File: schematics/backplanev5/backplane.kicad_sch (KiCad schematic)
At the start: 0 parts

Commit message: Update
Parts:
- added J1, J10, J2, J3, J4, J5, J6, J7, J8, J9: ~, ConnPdSilva:conn_euro96, symbol ConnPdSilva:ConnEuro96
- added J11, J12, J13, J14: Conn_01x02, Connector_PinHeader_2.54mm:PinHeader_2x01_P2.54mm_Vertical, symbol Connector_Generic:Conn_01x02
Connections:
- new net +12V: J1.92, J10.92, J13.1 (Pin_1), J2.92, J3.92, J4.92, J5.92, J6.92, J7.92, J8.92, J9.92
- new net +5V: J1.1, J1.33, J1.65, J10.1, J10.33, J10.65, J11.1 (Pin_1), J14.1 (Pin_1), J2.1, J2.33, J2.65, J3.1, J3.33, J3.65, J4.1, J4.33, J4.65, J5.1, J5.33, J5.65, J6.1, J6.33, J6.65, J7.1, J7.33, J7.65, J8.1, J8.33, J8.65, J9.1, J9.33, J9.65
- new net -5V: J1.94, J10.94, J12.1 (Pin_1), J2.94, J3.94, J4.94, J5.94, J6.94, J7.94, J8.94, J9.94
- new net A0: J1.18, J10.18, J2.18, J3.18, J4.18, J5.18, J6.18, J7.18, J8.18, J9.18
- new net A1: J1.19, J10.19, J2.19, J3.19, J4.19, J5.19, J6.19, J7.19, J8.19, J9.19
- new net A10: J1.28, J10.28, J2.28, J3.28, J4.28, J5.28, J6.28, J7.28, J8.28, J9.28
- new net A11: J1.29, J10.29, J2.29, J3.29, J4.29, J5.29, J6.29, J7.29, J8.29, J9.29
- new net A12: J1.30, J10.30, J2.30, J3.30, J4.30, J5.30, J6.30, J7.30, J8.30, J9.30
- new net A13: J1.31, J10.31, J2.31, J3.31, J4.31, J5.31, J6.31, J7.31, J8.31, J9.31
- new net A14: J1.63, J10.63, J2.63, J3.63, J4.63, J5.63, J6.63, J7.63, J8.63, J9.63
- new net A15: J1.62, J10.62, J2.62, J3.62, J4.62, J5.62, J6.62, J7.62, J8.62, J9.62
- new net A16: J1.61, J10.61, J2.61, J3.61, J4.61, J5.61, J6.61, J7.61, J8.61, J9.61
- new net A17: J1.60, J10.60, J2.60, J3.60, J4.60, J5.60, J6.60, J7.60, J8.60, J9.60
- new net A18: J1.59, J10.59, J2.59, J3.59, J4.59, J5.59, J6.59, J7.59, J8.59, J9.59
- new net A19: J1.58, J10.58, J2.58, J3.58, J4.58, J5.58, J6.58, J7.58, J8.58, J9.58
- new net A2: J1.20, J10.20, J2.20, J3.20, J4.20, J5.20, J6.20, J7.20, J8.20, J9.20
- new net A20: J1.57, J10.57, J2.57, J3.57, J4.57, J5.57, J6.57, J7.57, J8.57, J9.57
- new net A21: J1.56, J10.56, J2.56, J3.56, J4.56, J5.56, J6.56, J7.56, J8.56, J9.56
- new net A22: J1.55, J10.55, J2.55, J3.55, J4.55, J5.55, J6.55, J7.55, J8.55, J9.55
- new net A3: J1.21, J10.21, J2.21, J3.21, J4.21, J5.21, J6.21, J7.21, J8.21, J9.21
- new net A4: J1.22, J10.22, J2.22, J3.22, J4.22, J5.22, J6.22, J7.22, J8.22, J9.22
- new net A5: J1.23, J10.23, J2.23, J3.23, J4.23, J5.23, J6.23, J7.23, J8.23, J9.23
- new net A6: J1.24, J10.24, J2.24, J3.24, J4.24, J5.24, J6.24, J7.24, J8.24, J9.24
- new net A7: J1.25, J10.25, J2.25, J3.25, J4.25, J5.25, J6.25, J7.25, J8.25, J9.25
- new net A8: J1.26, J10.26, J2.26, J3.26, J4.26, J5.26, J6.26, J7.26, J8.26, J9.26
- new net A9: J1.27, J10.27, J2.27, J3.27, J4.27, J5.27, J6.27, J7.27, J8.27, J9.27
- new net ALE: J1.73, J10.73, J2.73, J3.73, J4.73, J5.73, J6.73, J7.73, J8.73, J9.73
- new net CRUCLK: J1.35, J10.35, J2.35, J3.35, J4.35, J5.35, J6.35, J7.35, J8.35, J9.35
- new net CRUIN: J1.36, J10.36, J2.36, J3.36, J4.36, J5.36, J6.36, J7.36, J8.36, J9.36
- new net CRUOUT: J1.37, J10.37, J2.37, J3.37, J4.37, J5.37, J6.37, J7.37, J8.37, J9.37
- new net D0: J1.2, J10.2, J2.2, J3.2, J4.2, J5.2, J6.2, J7.2, J8.2, J9.2
- new net D1: J1.3, J10.3, J2.3, J3.3, J4.3, J5.3, J6.3, J7.3, J8.3, J9.3
- new net D10: J1.12, J10.12, J2.12, J3.12, J4.12, J5.12, J6.12, J7.12, J8.12, J9.12
- new net D11: J1.13, J10.13, J2.13, J3.13, J4.13, J5.13, J6.13, J7.13, J8.13, J9.13
- new net D12: J1.14, J10.14, J2.14, J3.14, J4.14, J5.14, J6.14, J7.14, J8.14, J9.14
- new net D13: J1.15, J10.15, J2.15, J3.15, J4.15, J5.15, J6.15, J7.15, J8.15, J9.15
- new net D14: J1.16, J10.16, J2.16, J3.16, J4.16, J5.16, J6.16, J7.16, J8.16, J9.16
- new net D15: J1.17, J10.17, J2.17, J3.17, J4.17, J5.17, J6.17, J7.17, J8.17, J9.17
- new net D2: J1.4, J10.4, J2.4, J3.4, J4.4, J5.4, J6.4, J7.4, J8.4, J9.4
- new net D3: J1.5, J10.5, J2.5, J3.5, J4.5, J5.5, J6.5, J7.5, J8.5, J9.5
- new net D4: J1.6, J10.6, J2.6, J3.6, J4.6, J5.6, J6.6, J7.6, J8.6, J9.6
- new net D5: J1.7, J10.7, J2.7, J3.7, J4.7, J5.7, J6.7, J7.7, J8.7, J9.7
- new net D6: J1.8, J10.8, J2.8, J3.8, J4.8, J5.8, J6.8, J7.8, J8.8, J9.8
- new net D7: J1.9, J10.9, J2.9, J3.9, J4.9, J5.9, J6.9, J7.9, J8.9, J9.9
- new net D8: J1.10, J10.10, J2.10, J3.10, J4.10, J5.10, J6.10, J7.10, J8.10, J9.10
- new net D9: J1.11, J10.11, J2.11, J3.11, J4.11, J5.11, J6.11, J7.11, J8.11, J9.11
- new net DBIN: J1.38, J10.38, J2.38, J3.38, J4.38, J5.38, J6.38, J7.38, J8.38, J9.38
- new net DT/R: J1.75, J10.75, J2.75, J3.75, J4.75, J5.75, J6.75, J7.75, J8.75, J9.75
- new net E: J1.34, J10.34, J2.34, J3.34, J4.34, J5.34, J6.34, J7.34, J8.34, J9.34
- new net GND: J1.32, J1.64, J1.93, J1.95, J1.96, J10.32, J10.64, J10.93, J10.95, J10.96, J11.2 (Pin_2), J12.2 (Pin_2), J13.2 (Pin_2), J14.2 (Pin_2), J2.32, J2.64, J2.93, J2.95, J2.96, J3.32, J3.64, J3.93, J3.95, J3.96, J4.32, J4.64, J4.93, J4.95, J4.96, J5.32, J5.64, J5.93, J5.95, J5.96, J6.32, J6.64, J6.93, J6.95, J6.96, J7.32, J7.64, J7.93, J7.95, J7.96, J8.32, J8.64, J8.93, J8.95, J8.96, J9.32, J9.64, J9.93, J9.95, J9.96
- new net HLDA: J1.52, J10.52, J2.52, J3.52, J4.52, J5.52, J6.52, J7.52, J8.52, J9.52
- new net IAQ: J1.39, J10.39, J2.39, J3.39, J4.39, J5.39, J6.39, J7.39, J8.39, J9.39
- new net IC3: J1.47, J10.47, J2.47, J3.47, J4.47, J5.47, J6.47, J7.47, J8.47, J9.47
- new net IPL0: J1.50, J10.50, J2.50, J3.50, J4.50, J5.50, J6.50, J7.50, J8.50, J9.50
- new net IPL1: J1.49, J10.49, J2.49, J3.49, J4.49, J5.49, J6.49, J7.49, J8.49, J9.49
- new net IPL2: J1.48, J10.48, J2.48, J3.48, J4.48, J5.48, J6.48, J7.48, J8.48, J9.48
- new net M/IO: J1.76, J10.76, J2.76, J3.76, J4.76, J5.76, J6.76, J7.76, J8.76, J9.76
- new net NMI: J1.41, J10.41, J2.41, J3.41, J4.41, J5.41, J6.41, J7.41, J8.41, J9.41
- new net RDY: J1.44, J10.44, J2.44, J3.44, J4.44, J5.44, J6.44, J7.44, J8.44, J9.44
- new net Res1: J1.81, J10.81, J2.81, J3.81, J4.81, J5.81, J6.81, J7.81, J8.81, J9.81
- new net Res10: J1.90, J10.90, J2.90, J3.90, J4.90, J5.90, J6.90, J7.90, J8.90, J9.90
- new net Res11: J1.91, J10.91, J2.91, J3.91, J4.91, J5.91, J6.91, J7.91, J8.91, J9.91
- new net Res12: J1.54, J10.54, J2.54, J3.54, J4.54, J5.54, J6.54, J7.54, J8.54, J9.54
- new net Res2: J1.82, J10.82, J2.82, J3.82, J4.82, J5.82, J6.82, J7.82, J8.82, J9.82
- new net Res3: J1.83, J10.83, J2.83, J3.83, J4.83, J5.83, J6.83, J7.83, J8.83, J9.83
- new net Res4: J1.84, J10.84, J2.84, J3.84, J4.84, J5.84, J6.84, J7.84, J8.84, J9.84
- new net Res5: J1.85, J10.85, J2.85, J3.85, J4.85, J5.85, J6.85, J7.85, J8.85, J9.85
- new net Res6: J1.86, J10.86, J2.86, J3.86, J4.86, J5.86, J6.86, J7.86, J8.86, J9.86
- new net Res7: J1.87, J10.87, J2.87, J3.87, J4.87, J5.87, J6.87, J7.87, J8.87, J9.87
- new net Res8: J1.88, J10.88, J2.88, J3.88, J4.88, J5.88, J6.88, J7.88, J8.88, J9.88
- new net Res9: J1.89, J10.89, J2.89, J3.89, J4.89, J5.89, J6.89, J7.89, J8.89, J9.89
- new net /AS: J1.43, J10.43, J2.43, J3.43, J4.43, J5.43, J6.43, J7.43, J8.43, J9.43
- new net /BERR: J1.68, J10.68, J2.68, J3.68, J4.68, J5.68, J6.68, J7.68, J8.68, J9.68
- new net /BGACK: J1.69, J10.69, J2.69, J3.69, J4.69, J5.69, J6.69, J7.69, J8.69, J9.69
- new net /DEN: J1.74, J10.74, J2.74, J3.74, J4.74, J5.74, J6.74, J7.74, J8.74, J9.74
- new net /HALT: J1.53, J10.53, J2.53, J3.53, J4.53, J5.53, J6.53, J7.53, J8.53, J9.53
- new net /HOLD: J1.42, J10.42, J2.42, J3.42, J4.42, J5.42, J6.42, J7.42, J8.42, J9.42
- new net /INTA: J1.72, J10.72, J2.72, J3.72, J4.72, J5.72, J6.72, J7.72, J8.72, J9.72
- new net /INTR: J1.40, J10.40, J2.40, J3.40, J4.40, J5.40, J6.40, J7.40, J8.40, J9.40
- new net /LDS: J1.70, J10.70, J2.70, J3.70, J4.70, J5.70, J6.70, J7.70, J8.70, J9.70
- new net /M1: J1.79, J10.79, J2.79, J3.79, J4.79, J5.79, J6.79, J7.79, J8.79, J9.79
- new net /RD: J1.45, J10.45, J2.45, J3.45, J4.45, J5.45, J6.45, J7.45, J8.45, J9.45
- new net /RFSH: J1.80, J10.80, J2.80, J3.80, J4.80, J5.80, J6.80, J7.80, J8.80, J9.80
- new net /RST: J1.51, J10.51, J2.51, J3.51, J4.51, J5.51, J6.51, J7.51, J8.51, J9.51
- new net /SSO: J1.77, J10.77, J2.77, J3.77, J4.77, J5.77, J6.77, J7.77, J8.77, J9.77
- new net /UDS: J1.71, J10.71, J2.71, J3.71, J4.71, J5.71, J6.71, J7.71, J8.71, J9.71
- new net /VMA: J1.66, J10.66, J2.66, J3.66, J4.66, J5.66, J6.66, J7.66, J8.66, J9.66
- new net /VPA: J1.67, J10.67, J2.67, J3.67, J4.67, J5.67, J6.67, J7.67, J8.67, J9.67
- new net /WAIT: J1.78, J10.78, J2.78, J3.78, J4.78, J5.78, J6.78, J7.78, J8.78, J9.78
- new net /WE: J1.46, J10.46, J2.46, J3.46, J4.46, J5.46, J6.46, J7.46, J8.46, J9.46

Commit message: Update V1 fabrication 04-12-2025 JLCPCB
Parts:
- added H1, H2, H3, H4, H5, H6: MountingHole, MountingHole:MountingHole_3.2mm_M3, symbol Mechanical:MountingHole

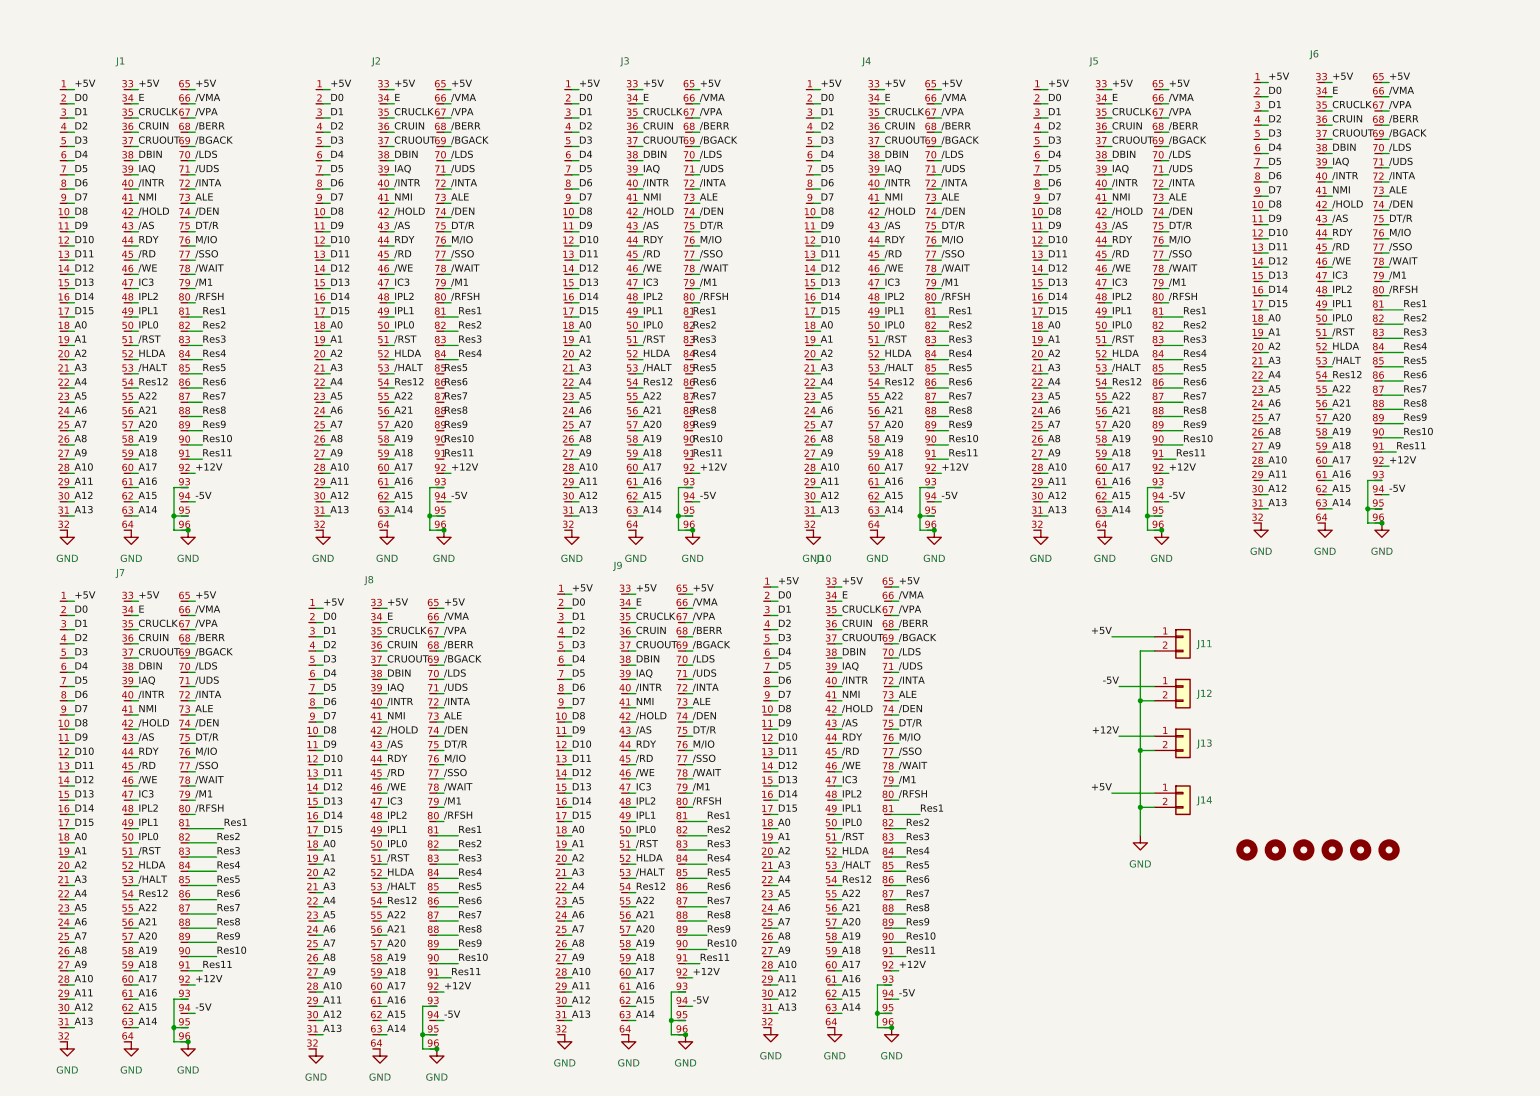
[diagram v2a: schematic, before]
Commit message: Terminada as mudancas falta agora fazer oDRC
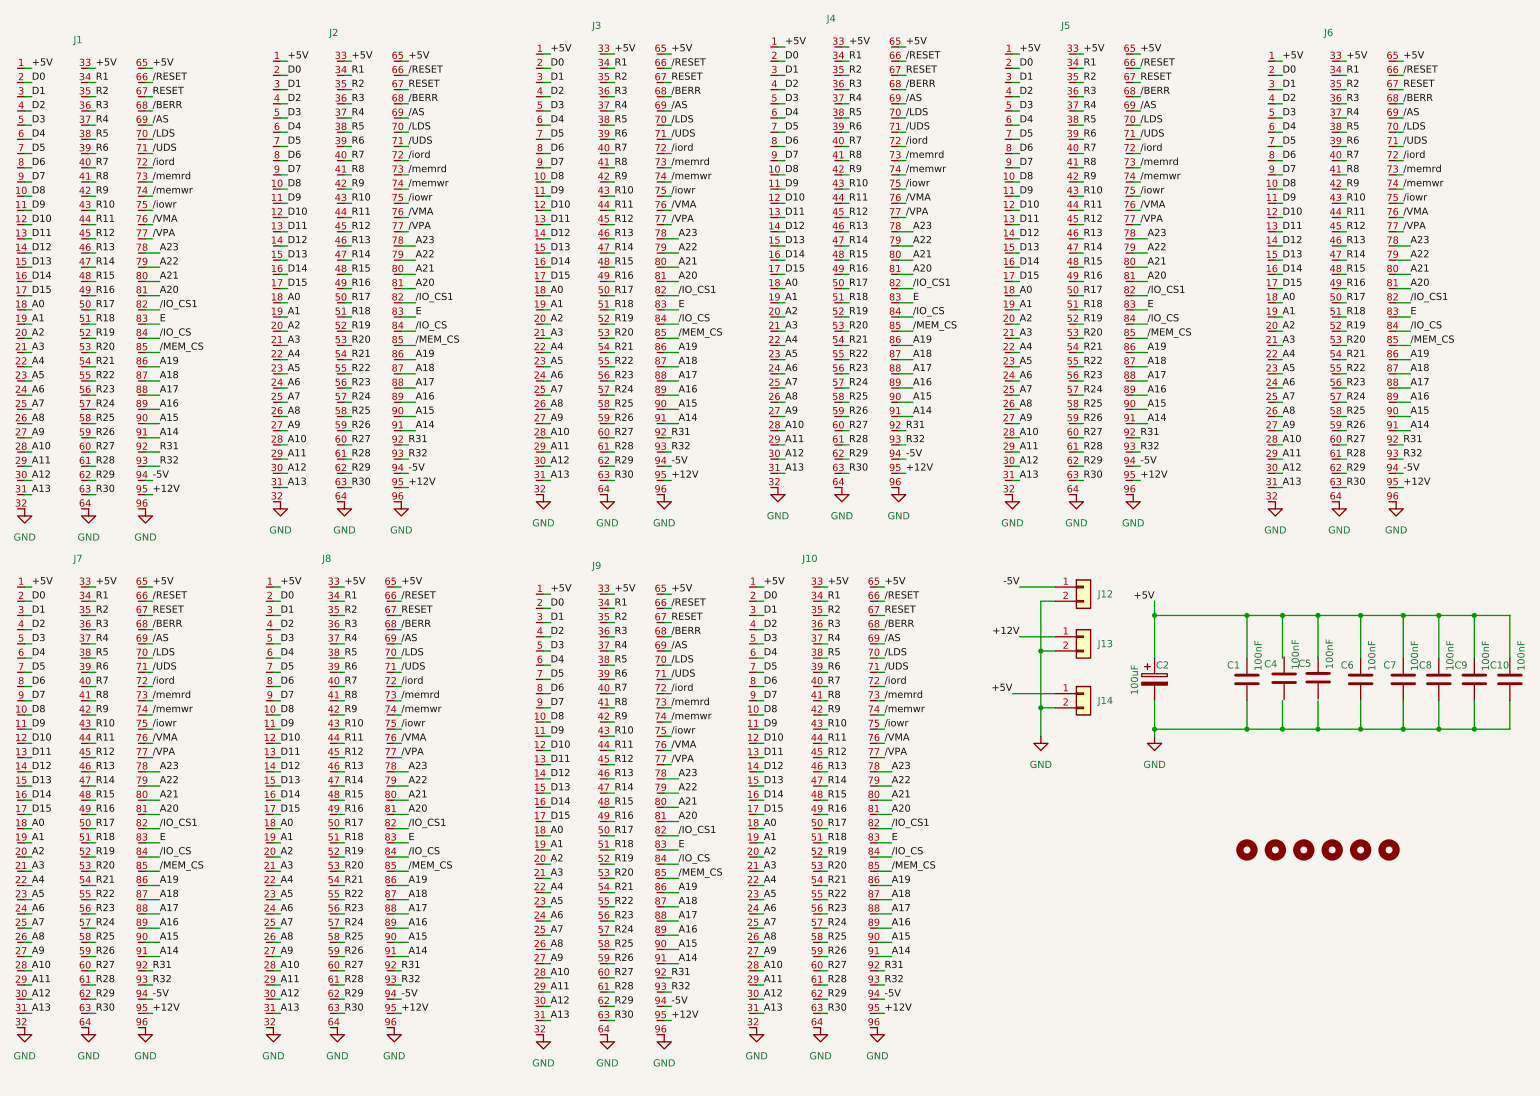
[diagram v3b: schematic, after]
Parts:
- removed J11: Conn_01x02, Connector_PinHeader_2.54mm:PinHeader_2x01_P2.54mm_Vertical, symbol Connector_Generic:Conn_01x02
- added C1, C10, C4, C5, C6, C7, C8, C9: 100nF, Capacitor_THT:C_Disc_D4.3mm_W1.9mm_P5.00mm, symbol Device:C
- added C2: 100uF, Capacitor_THT:CP_Radial_D8.0mm_P5.00mm, symbol Device:C_Polarized
- J12, J13, J14: footprint Connector_PinHeader_2.54mm:PinHeader_2x01_P2.54mm_Vertical -> TerminalBlock_Phoenix:TerminalBlock_Phoenix_MKDS-1,5-2-5.08_1x02_P5.08mm_Horizontal
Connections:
- net M/IO is gone; now on net /VMA: J1.76, J10.76, J2.76, J3.76, J4.76, J5.76, J6.76, J7.76, J8.76, J9.76
- net Res1 is gone; now on net A20: J1.81, J10.81, J2.81, J3.81, J4.81, J5.81, J6.81, J7.81, J8.81, J9.81
- net Res10 is gone; now on net A15: J1.90, J10.90, J2.90, J3.90, J4.90, J5.90, J6.90, J7.90, J8.90, J9.90
- net Res11 is gone; now on net A14: J1.91, J10.91, J2.91, J3.91, J4.91, J5.91, J6.91, J7.91, J8.91, J9.91
- net Res3 is gone; now on net E: J1.83, J10.83, J2.83, J3.83, J4.83, J5.83, J6.83, J7.83, J8.83, J9.83
- net Res6 is gone; now on net A19: J1.86, J10.86, J2.86, J3.86, J4.86, J5.86, J6.86, J7.86, J8.86, J9.86
- net Res7 is gone; now on net A18: J1.87, J10.87, J2.87, J3.87, J4.87, J5.87, J6.87, J7.87, J8.87, J9.87
- net Res8 is gone; now on net A17: J1.88, J10.88, J2.88, J3.88, J4.88, J5.88, J6.88, J7.88, J8.88, J9.88
- net Res9 is gone; now on net A16: J1.89, J10.89, J2.89, J3.89, J4.89, J5.89, J6.89, J7.89, J8.89, J9.89
- net /BGACK is gone; now on net /AS: J1.69, J10.69, J2.69, J3.69, J4.69, J5.69, J6.69, J7.69, J8.69, J9.69
- net /M1 is gone; now on net A22: J1.79, J10.79, J2.79, J3.79, J4.79, J5.79, J6.79, J7.79, J8.79, J9.79
- net /RFSH is gone; now on net A21: J1.80, J10.80, J2.80, J3.80, J4.80, J5.80, J6.80, J7.80, J8.80, J9.80
- net /SSO is gone; now on net /VPA: J1.77, J10.77, J2.77, J3.77, J4.77, J5.77, J6.77, J7.77, J8.77, J9.77
- net +12V: now also J1.95, J10.95, J2.95, J3.95, J4.95, J5.95, J6.95, J7.95, J8.95, J9.95; no longer J1.92, J10.92, J2.92, J3.92, J4.92, J5.92, J6.92, J7.92, J8.92, J9.92
- net +5V: now also C1.1, C10.1, C2.1, C6.1, C7.1, C8.1, C9.1
- net A14: no longer J1.63, J10.63, J2.63, J3.63, J4.63, J5.63, J6.63, J7.63, J8.63, J9.63
- net A15: no longer J1.62, J10.62, J2.62, J3.62, J4.62, J5.62, J6.62, J7.62, J8.62, J9.62
- net A16: no longer J1.61, J10.61, J2.61, J3.61, J4.61, J5.61, J6.61, J7.61, J8.61, J9.61
- net A17: no longer J1.60, J10.60, J2.60, J3.60, J4.60, J5.60, J6.60, J7.60, J8.60, J9.60
- net A18: no longer J1.59, J10.59, J2.59, J3.59, J4.59, J5.59, J6.59, J7.59, J8.59, J9.59
- net A19: no longer J1.58, J10.58, J2.58, J3.58, J4.58, J5.58, J6.58, J7.58, J8.58, J9.58
- net A20: no longer J1.57, J10.57, J2.57, J3.57, J4.57, J5.57, J6.57, J7.57, J8.57, J9.57
- net A21: no longer J1.56, J10.56, J2.56, J3.56, J4.56, J5.56, J6.56, J7.56, J8.56, J9.56
- net A22: no longer J1.55, J10.55, J2.55, J3.55, J4.55, J5.55, J6.55, J7.55, J8.55, J9.55
- net E: no longer J1.34, J10.34, J2.34, J3.34, J4.34, J5.34, J6.34, J7.34, J8.34, J9.34
- net GND: now also C1.2, C10.2, C2.2, C6.2, C7.2, C8.2, C9.2; no longer J1.93, J1.95, J10.93, J10.95, J2.93, J2.95, J3.93, J3.95, J4.93, J4.95, J5.93, J5.95, J6.93, J6.95, J7.93, J7.95, J8.93, J8.95, J9.93, J9.95
- net /AS: no longer J1.43, J10.43, J2.43, J3.43, J4.43, J5.43, J6.43, J7.43, J8.43, J9.43
- net /VMA: no longer J1.66, J10.66, J2.66, J3.66, J4.66, J5.66, J6.66, J7.66, J8.66, J9.66
- net /VPA: no longer J1.67, J10.67, J2.67, J3.67, J4.67, J5.67, J6.67, J7.67, J8.67, J9.67
- net ALE renamed /memrd
- net CRUCLK renamed R2
- net CRUIN renamed R3
- net CRUOUT renamed R4
- net DBIN renamed R5
- net DT/R renamed /iowr
- net HLDA renamed R19
- net IAQ renamed R6
- net IC3 renamed R14
- net IPL0 renamed R17
- net IPL1 renamed R16
- net IPL2 renamed R15
- net NMI renamed R8
- net RDY renamed R11
- net Res12 renamed R21
- net Res2 renamed /IO_CS1
- net Res4 renamed /IO_CS
- net Res5 renamed /MEM_CS
- net /DEN renamed /memwr
- net /HALT renamed R20
- net /HOLD renamed R9
- net /INTA renamed /iord
- net /INTR renamed R7
- net /RD renamed R12
- net /RST renamed R18
- net /WAIT renamed A23
- net /WE renamed R13
- new net R1: J1.34, J10.34, J2.34, J3.34, J4.34, J5.34, J6.34, J7.34, J8.34, J9.34
- new net R10: J1.43, J10.43, J2.43, J3.43, J4.43, J5.43, J6.43, J7.43, J8.43, J9.43
- new net R22: J1.55, J10.55, J2.55, J3.55, J4.55, J5.55, J6.55, J7.55, J8.55, J9.55
- new net R23: J1.56, J10.56, J2.56, J3.56, J4.56, J5.56, J6.56, J7.56, J8.56, J9.56
- new net R24: J1.57, J10.57, J2.57, J3.57, J4.57, J5.57, J6.57, J7.57, J8.57, J9.57
- new net R25: J1.58, J10.58, J2.58, J3.58, J4.58, J5.58, J6.58, J7.58, J8.58, J9.58
- new net R26: J1.59, J10.59, J2.59, J3.59, J4.59, J5.59, J6.59, J7.59, J8.59, J9.59
- new net R27: J1.60, J10.60, J2.60, J3.60, J4.60, J5.60, J6.60, J7.60, J8.60, J9.60
- new net R28: J1.61, J10.61, J2.61, J3.61, J4.61, J5.61, J6.61, J7.61, J8.61, J9.61
- new net R29: J1.62, J10.62, J2.62, J3.62, J4.62, J5.62, J6.62, J7.62, J8.62, J9.62
- new net R30: J1.63, J10.63, J2.63, J3.63, J4.63, J5.63, J6.63, J7.63, J8.63, J9.63
- new net R31: J1.92, J10.92, J2.92, J3.92, J4.92, J5.92, J6.92, J7.92, J8.92, J9.92
- new net R32: J1.93, J10.93, J2.93, J3.93, J4.93, J5.93, J6.93, J7.93, J8.93, J9.93
- new net RESET: J1.67, J10.67, J2.67, J3.67, J4.67, J5.67, J6.67, J7.67, J8.67, J9.67
- new net /RESET: J1.66, J10.66, J2.66, J3.66, J4.66, J5.66, J6.66, J7.66, J8.66, J9.66
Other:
- moved on the sheet: J1, J12, J13, J14

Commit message: Terminado o DRC
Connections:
- net +5V: now also C4.1, C5.1
- net GND: now also C4.2, C5.2
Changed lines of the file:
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@@
 	(symbol
 		(lib_id "Device:C")
-		(at 246.41 127.9638 0)
+		(at 246.38 128.27 0)
 		(unit 1)
 		(exclude_from_sim no)
@@
 		(dnp no)
 		(property "Reference" "C5"
-			(at 242.854 125.4238 0)
+			(at 242.824 125.73 0)
 			(effects
 				(font
@@
 		)
 		(property "Value" "100nF"
-			(at 248.442 126.4398 90)
+			(at 248.412 126.746 90)
 			(effects
 				(font
@@
 		)
 		(property "Footprint" "Capacitor_THT:C_Disc_D4.3mm_W1.9mm_P5.00mm"
-			(at 247.3752 131.7738 0)
+			(at 247.3452 132.08 0)
 			(effects
 				(font
@@
 		)
 		(property "Datasheet" "~"
-			(at 246.41 127.9638 0)
+			(at 246.38 128.27 0)
 			(effects
 				(font
@@
 		)
 		(property "Description" "Unpolarized capacitor"
-			(at 246.41 127.9638 0)
+			(at 246.38 128.27 0)
 			(effects
 				(font
@@
 	(symbol
 		(lib_id "Device:C")
-		(at 240.3251 128.0619 0)
+		(at 240.03 128.27 0)
 		(unit 1)
 		(exclude_from_sim no)
@@
 		(dnp no)
 		(property "Reference" "C4"
-			(at 236.7691 125.5219 0)
+			(at 236.474 125.73 0)
 			(effects
 				(font
@@
 		)
 		(property "Value" "100nF"
-			(at 242.3571 126.5379 90)
+			(at 242.062 126.746 90)
 			(effects
 				(font
@@
 		)
 		(property "Footprint" "Capacitor_THT:C_Disc_D4.3mm_W1.9mm_P5.00mm"
-			(at 241.2903 131.8719 0)
+			(at 240.9952 132.08 0)
 			(effects
 				(font
@@
 		)
 		(property "Datasheet" "~"
-			(at 240.3251 128.0619 0)
+			(at 240.03 128.27 0)
 			(effects
 				(font
@@
 		)
 		(property "Description" "Unpolarized capacitor"
-			(at 240.3251 128.0619 0)
-			(effects
-				(font
+			(at 240.03 128.27 0)
+			(effects
+				(font
